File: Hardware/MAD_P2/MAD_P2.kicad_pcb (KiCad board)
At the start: 4 copper layers, 121.6 x 145.5 mm, 363 parts, among them J1 Line_1_3, J10 Conn_02x05_Odd_Even, J11 Conn_02x05_Odd_Even, J12 Line_3_3, J13 Conn_02x05_Odd_Even, J14 Conn_02x05_Odd_Even, J15 Conn_ADC1, J16 Conn_DAC, J17 Line_1_2, J18 P3, J19 P4, J2 Line_2_2, J20 P2, J21 Conn_02x05_Odd_Even, J22 Conn_02x05_Odd_Even, J23 Conn_02x03_Odd_Even, J24 P5, J25 P6, J26 P7, J27 Line_1_1, J28 Line_2_1, J29 Line_2_3, J3 Line_3_1, J30 Line_3_2, J31 Micro_SD_Card_Connector, J32 Micro_SD_Card_Socket, J33 Shifted IO, J4 Power_In, J5 Micro_SD_Card, J6 Edge_Conn, J7 Conn_02x05_Odd_Even, J8 USB_C_Receptacle_USB2.0, J9 Conn_02x05_Odd_Even, P10 CONN_01X01, P11 CONN_01X01, P13 CONN_01X01, P8 CONN_01X01, Q1 MMBT3904, Q2 2N7002, Q3 2N7002, Q4 2N7002, Q5 2N7002, SW1 Switch_SW_Push, U1 P2X8C4M64P-REF, U10 AMS1117-3.3, U11 APM4953, U12 APM4953, U13 XL1509-5.0, U14 XL1509-5.0, U15 AMS1117-3.3, U16 AMS1117-3.3, U17 MAX5134-7, U18 AMS1117-3.3, U19 AMS1117-1.8, U2 XL1509-5.0, U20 LM321, U21 APM4953, U22 XL1509-5.0, U23 ADS131A04, U24 AMS1117-3.3, U26 W25Q128JVS, U27 FT232RL, U28 DS3231M, U29 ESP-12F, U3 XL1509-5.0, U4 XL1509-5.0, U5 XL1509-5.0, U6 AMS1117-3.3, U7 AMS1117-3.3, U8 AMS1117-3.3, U9 AMS1117-3.3, Y1 20MHz, Y2 16.384MHz

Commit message: begining autorouter, had to start again after edge connector footprint was incorrect
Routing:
- net P22: track 0.00 -> 4.75 mm, vias 0 -> 1
- net GND: track 623.8 -> 619.0 mm, vias 343 -> 342
- net Net-(J8-PadA6): track 4.29 -> 6.99 mm
- net Net-(J8-PadA7): track 3.03 -> 5.73 mm

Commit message: added boarders along keep out zones for autorouter:
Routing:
- net (no net): track 0.00 -> 698.4 mm
- added copper zone on In1.Cu, net (none)
- removed copper zone on In1.Cu, net +1V8
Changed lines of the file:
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@@
     (thickness 1.6)
     (drawings 126)
-    (tracks 3104)
+    (tracks 3168)
     (zones 0)
     (modules 363)
@@
   (gr_line (start 514 160.867) (end 514 15.367) (layer Edge.Cuts) (width 0.05))
   (gr_line (start 392.43 160.867) (end 514 160.867) (layer Edge.Cuts) (width 0.05))
+  (segment (start 407.67 130.573166) (end 407.797 130.446166) (width 0.25) (layer F.Cu) (net 0))
+  (segment (start 407.67 153.67) (end 407.67 130.573166) (width 0.25) (layer F.Cu) (net 0))
+  (segment (start 407.797 130.446166) (end 407.797 120.5865) (width 0.25) (layer F.Cu) (net 0))
+  (segment (start 431.927 160.274) (end 431.927 156.0195) (width 0.25) (layer F.Cu) (net 0))
+  (segment (start 431.927 156.0195) (end 432.562 155.3845) (width 0.25) (layer F.Cu) (net 0))
+  (segment (start 432.562 155.3845) (end 432.562 118.5545) (width 0.25) (layer F.Cu) (net 0))
+  (segment (start 432.435 117.094) (end 410.6545 117.094) (width 0.25) (layer F.Cu) (net 0))
+  (segment (start 407.67 130.573166) (end 407.797 130.446166) (width 0.25) (layer F.Cu) (net 0))
+  (segment (start 432.435 117.094) (end 410.6545 117.094) (width 0.25) (layer F.Cu) (net 0))
+  (segment (start 432.562 155.3845) (end 432.562 118.5545) (width 0.25) (layer F.Cu) (net 0))
+  (segment (start 407.67 153.67) (end 407.67 130.573166) (width 0.25) (layer F.Cu) (net 0))
+  (segment (start 407.797 130.446166) (end 407.797 120.5865) (width 0.25) (layer F.Cu) (net 0))
+  (segment (start 407.8605 153.67) (end 407.8605 117.2845) (width 0.25) (layer In1.Cu) (net 0))
+  (segment (start 407.8605 117.2845) (end 432.3715 117.2845) (width 0.25) (layer In1.Cu) (net 0))
+  (segment (start 432.91649 117.82949) (end 432.91649 133.18601) (width 0.25) (layer In1.Cu) (net 0))
+  (segment (start 432.3715 117.2845) (end 432.91649 117.82949) (width 0.25) (layer In1.Cu) (net 0))
+  (segment (start 432.91649 151.874808) (end 431.8635 152.927798) (width 0.25) (layer In1.Cu) (net 0))
+  (segment (start 432.91649 133.18601) (end 432.91649 151.874808) (width 0.25) (layer In1.Cu) (net 0))
+  (segment (start 431.8635 152.927798) (end 431.8635 160.0835) (width 0.25) (layer In1.Cu) (net 0))
+  (segment (start 407.4795 144.278498) (end 407.8605 143.897498) (width 0.25) (layer In2.Cu) (net 0))
+  (segment (start 407.4795 153.7335) (end 407.4795 144.278498) (width 0.25) (layer In2.Cu) (net 0))
+  (segment (start 407.8605 143.897498) (end 407.8605 119.247498) (width 0.25) (layer In2.Cu) (net 0))
+  (segment (start 407.8605 119.247498) (end 409.823498 117.2845) (width 0.25) (layer In2.Cu) (net 0))
+  (segment (start 409.823498 117.2845) (end 432.4985 117.2845) (width 0.25) (layer In2.Cu) (net 0))
+  (segment (start 432.4985 118.230502) (end 432.7525 118.484502) (width 0.25) (layer In2.Cu) (net 0))
+  (segment (start 432.4985 117.2845) (end 432.4985 118.230502) (width 0.25) (layer In2.Cu) (net 0))
+  (segment (start 432.7525 159.639) (end 431.87451 160.51699) (width 0.25) (layer In2.Cu) (net 0))
+  (segment (start 432.7525 118.484502) (end 432.7525 159.639) (width 0.25) (layer In2.Cu) (net 0))
+  (segment (start 407.797 154.1145) (end 407.797 127.831998) (width 0.25) (layer B.Cu) (net 0))
+  (segment (start 407.797 119.310998) (end 409.823498 117.2845) (width 0.25) (layer B.Cu) (net 0))
+  (segment (start 407.797 127.831998) (end 407.797 119.310998) (width 0.25) (layer B.Cu) (net 0))
+  (segment (start 409.823498 117.2845) (end 432.054 117.2845) (width 0.25) (layer B.Cu) (net 0))
+  (segment (start 432.537501 117.768001) (end 432.537501 159.028499) (width 0.25) (layer B.Cu) (net 0))
+  (segment (start 432.054 117.2845) (end 432.537501 117.768001) (width 0.25) (layer B.Cu) (net 0))
+  (segment (start 452.4375 135.6995) (end 445.262 135.6995) (width 0.25) (layer B.Cu) (net 0))
+  (segment (start 445.262 135.6995) (end 445.262 116.1415) (width 0.25) (layer B.Cu) (net 0))
+  (segment (start 445.362499 116.041001) (end 464.910001 116.041001) (width 0.25) (layer B.Cu) (net 0))
+  (segment (start 445.262 116.1415) (end 445.362499 116.041001) (width 0.25) (layer B.Cu) (net 0))
+  (segment (start 464.910001 116.041001) (end 465.201 116.332) (width 0.25) (layer B.Cu) (net 0))
+  (segment (start 465.201 131.372002) (end 465.1375 131.435502) (width 0.25) (layer B.Cu) (net 0))
+  (segment (start 465.201 116.332) (end 465.201 131.372002) (width 0.25) (layer B.Cu) (net 0))
+  (segment (start 465.1375 131.435502) (end 465.1375 135.5725) (width 0.25) (layer B.Cu) (net 0))
+  (segment (start 465.1375 135.5725) (end 457.327 135.5725) (width 0.25) (layer B.Cu) (net 0))
+  (segment (start 452.755 135.763) (end 445.262 135.763) (width 0.25) (layer In2.Cu) (net 0))
+  (segment (start 445.262 135.763) (end 445.135 135.636) (width 0.25) (layer In2.Cu) (net 0))
+  (segment (start 445.135 122.612998) (end 451.669998 116.078) (width 0.25) (layer In2.Cu) (net 0))
+  (segment (start 445.135 135.636) (end 445.135 122.612998) (width 0.25) (layer In2.Cu) (net 0))
+  (segment (start 451.669998 116.078) (end 458.794002 116.078) (width 0.25) (layer In2.Cu) (net 0))
+  (segment (start 458.794002 116.078) (end 458.921002 116.205) (width 0.25) (layer In2.Cu) (net 0))
+  (segment (start 458.921002 116.205) (end 465.2645 116.205) (width 0.25) (layer In2.Cu) (net 0))
+  (segment (start 465.2645 116.205) (end 465.0105 116.459) (width 0.25) (layer In2.Cu) (net 0))
+  (segment (start 465.0105 116.459) (end 465.0105 131.562502) (width 0.25) (layer In2.Cu) (net 0))
+  (segment (start 465.0105 131.562502) (end 465.0105 135.382) (width 0.25) (layer In2.Cu) (net 0))
+  (segment (start 465.0105 135.382) (end 464.693 135.6995) (width 0.25) (layer In2.Cu) (net 0))
+  (segment (start 464.693 135.6995) (end 457.327 135.6995) (width 0.25) (layer In2.Cu) (net 0))
+  (segment (start 452.755 136.0805) (end 445.262 136.0805) (width 0.25) (layer F.Cu) (net 0))
+  (segment (start 457.3905 136.144) (end 464.947 136.144) (width 0.25) (layer F.Cu) (net 0))
+  (segment (start 464.947 136.144) (end 465.836 135.255) (width 0.25) (layer F.Cu) (net 0))
+  (segment (start 465.836 135.255) (end 465.836 122.483588) (width 0.25) (layer F.Cu) (net 0))
+  (segment (start 465.836 122.483588) (end 465.836 117.1575) (width 0.25) (layer F.Cu) (net 0))
+  (segment (start 453.733412 116.84) (end 453.542912 117.0305) (width 0.25) (layer F.Cu) (net 0))
+  (segment (start 465.5185 116.84) (end 453.733412 116.84) (width 0.25) (layer F.Cu) (net 0))
+  (segment (start 465.836 117.1575) (end 465.5185 116.84) (width 0.25) (layer F.Cu) (net 0))
+  (segment (start 453.542912 117.0305) (end 445.3255 117.0305) (width 0.25) (layer F.Cu) (net 0))
   (via (at 479.8125 144.9375) (size 0.8) (drill 0.4) (layers F.Cu B.Cu) (net 1))
   (segment (start 472.91699 138.04199) (end 479.8125 144.9375) (width 0.25) (layer F.Cu) (net 1))
@@
     )
   )
-  (zone (net 3) (net_name +1V8) (layer In1.Cu) (hatch edge 0.508)
+  (zone (net 0) (net_name "") (layer In1.Cu) (hatch edge 0.508)
     (connect_pads (clearance 0.508))
     (min_thickness 0.254)

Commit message: added keepout areas to adc/dac
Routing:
- net (no net): track 698.4 -> 0.00 mm
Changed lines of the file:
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@@
     (thickness 1.6)
     (drawings 126)
-    (tracks 3168)
+    (tracks 3104)
     (zones 0)
     (modules 363)
@@
   (gr_line (start 514 160.867) (end 514 15.367) (layer Edge.Cuts) (width 0.05))
   (gr_line (start 392.43 160.867) (end 514 160.867) (layer Edge.Cuts) (width 0.05))
-  (segment (start 407.67 130.573166) (end 407.797 130.446166) (width 0.25) (layer F.Cu) (net 0))
-  (segment (start 407.67 153.67) (end 407.67 130.573166) (width 0.25) (layer F.Cu) (net 0))
-  (segment (start 407.797 130.446166) (end 407.797 120.5865) (width 0.25) (layer F.Cu) (net 0))
-  (segment (start 431.927 160.274) (end 431.927 156.0195) (width 0.25) (layer F.Cu) (net 0))
-  (segment (start 431.927 156.0195) (end 432.562 155.3845) (width 0.25) (layer F.Cu) (net 0))
-  (segment (start 432.562 155.3845) (end 432.562 118.5545) (width 0.25) (layer F.Cu) (net 0))
-  (segment (start 432.435 117.094) (end 410.6545 117.094) (width 0.25) (layer F.Cu) (net 0))
-  (segment (start 407.67 130.573166) (end 407.797 130.446166) (width 0.25) (layer F.Cu) (net 0))
-  (segment (start 432.435 117.094) (end 410.6545 117.094) (width 0.25) (layer F.Cu) (net 0))
-  (segment (start 432.562 155.3845) (end 432.562 118.5545) (width 0.25) (layer F.Cu) (net 0))
-  (segment (start 407.67 153.67) (end 407.67 130.573166) (width 0.25) (layer F.Cu) (net 0))
-  (segment (start 407.797 130.446166) (end 407.797 120.5865) (width 0.25) (layer F.Cu) (net 0))
-  (segment (start 407.8605 153.67) (end 407.8605 117.2845) (width 0.25) (layer In1.Cu) (net 0))
-  (segment (start 407.8605 117.2845) (end 432.3715 117.2845) (width 0.25) (layer In1.Cu) (net 0))
-  (segment (start 432.91649 117.82949) (end 432.91649 133.18601) (width 0.25) (layer In1.Cu) (net 0))
-  (segment (start 432.3715 117.2845) (end 432.91649 117.82949) (width 0.25) (layer In1.Cu) (net 0))
-  (segment (start 432.91649 151.874808) (end 431.8635 152.927798) (width 0.25) (layer In1.Cu) (net 0))
-  (segment (start 432.91649 133.18601) (end 432.91649 151.874808) (width 0.25) (layer In1.Cu) (net 0))
-  (segment (start 431.8635 152.927798) (end 431.8635 160.0835) (width 0.25) (layer In1.Cu) (net 0))
-  (segment (start 407.4795 144.278498) (end 407.8605 143.897498) (width 0.25) (layer In2.Cu) (net 0))
-  (segment (start 407.4795 153.7335) (end 407.4795 144.278498) (width 0.25) (layer In2.Cu) (net 0))
-  (segment (start 407.8605 143.897498) (end 407.8605 119.247498) (width 0.25) (layer In2.Cu) (net 0))
-  (segment (start 407.8605 119.247498) (end 409.823498 117.2845) (width 0.25) (layer In2.Cu) (net 0))
-  (segment (start 409.823498 117.2845) (end 432.4985 117.2845) (width 0.25) (layer In2.Cu) (net 0))
-  (segment (start 432.4985 118.230502) (end 432.7525 118.484502) (width 0.25) (layer In2.Cu) (net 0))
-  (segment (start 432.4985 117.2845) (end 432.4985 118.230502) (width 0.25) (layer In2.Cu) (net 0))
-  (segment (start 432.7525 159.639) (end 431.87451 160.51699) (width 0.25) (layer In2.Cu) (net 0))
-  (segment (start 432.7525 118.484502) (end 432.7525 159.639) (width 0.25) (layer In2.Cu) (net 0))
-  (segment (start 407.797 154.1145) (end 407.797 127.831998) (width 0.25) (layer B.Cu) (net 0))
-  (segment (start 407.797 119.310998) (end 409.823498 117.2845) (width 0.25) (layer B.Cu) (net 0))
-  (segment (start 407.797 127.831998) (end 407.797 119.310998) (width 0.25) (layer B.Cu) (net 0))
-  (segment (start 409.823498 117.2845) (end 432.054 117.2845) (width 0.25) (layer B.Cu) (net 0))
-  (segment (start 432.537501 117.768001) (end 432.537501 159.028499) (width 0.25) (layer B.Cu) (net 0))
-  (segment (start 432.054 117.2845) (end 432.537501 117.768001) (width 0.25) (layer B.Cu) (net 0))
-  (segment (start 452.4375 135.6995) (end 445.262 135.6995) (width 0.25) (layer B.Cu) (net 0))
-  (segment (start 445.262 135.6995) (end 445.262 116.1415) (width 0.25) (layer B.Cu) (net 0))
-  (segment (start 445.362499 116.041001) (end 464.910001 116.041001) (width 0.25) (layer B.Cu) (net 0))
-  (segment (start 445.262 116.1415) (end 445.362499 116.041001) (width 0.25) (layer B.Cu) (net 0))
-  (segment (start 464.910001 116.041001) (end 465.201 116.332) (width 0.25) (layer B.Cu) (net 0))
-  (segment (start 465.201 131.372002) (end 465.1375 131.435502) (width 0.25) (layer B.Cu) (net 0))
-  (segment (start 465.201 116.332) (end 465.201 131.372002) (width 0.25) (layer B.Cu) (net 0))
-  (segment (start 465.1375 131.435502) (end 465.1375 135.5725) (width 0.25) (layer B.Cu) (net 0))
-  (segment (start 465.1375 135.5725) (end 457.327 135.5725) (width 0.25) (layer B.Cu) (net 0))
-  (segment (start 452.755 135.763) (end 445.262 135.763) (width 0.25) (layer In2.Cu) (net 0))
-  (segment (start 445.262 135.763) (end 445.135 135.636) (width 0.25) (layer In2.Cu) (net 0))
-  (segment (start 445.135 122.612998) (end 451.669998 116.078) (width 0.25) (layer In2.Cu) (net 0))
-  (segment (start 445.135 135.636) (end 445.135 122.612998) (width 0.25) (layer In2.Cu) (net 0))
-  (segment (start 451.669998 116.078) (end 458.794002 116.078) (width 0.25) (layer In2.Cu) (net 0))
-  (segment (start 458.794002 116.078) (end 458.921002 116.205) (width 0.25) (layer In2.Cu) (net 0))
-  (segment (start 458.921002 116.205) (end 465.2645 116.205) (width 0.25) (layer In2.Cu) (net 0))
-  (segment (start 465.2645 116.205) (end 465.0105 116.459) (width 0.25) (layer In2.Cu) (net 0))
-  (segment (start 465.0105 116.459) (end 465.0105 131.562502) (width 0.25) (layer In2.Cu) (net 0))
-  (segment (start 465.0105 131.562502) (end 465.0105 135.382) (width 0.25) (layer In2.Cu) (net 0))
-  (segment (start 465.0105 135.382) (end 464.693 135.6995) (width 0.25) (layer In2.Cu) (net 0))
-  (segment (start 464.693 135.6995) (end 457.327 135.6995) (width 0.25) (layer In2.Cu) (net 0))
-  (segment (start 452.755 136.0805) (end 445.262 136.0805) (width 0.25) (layer F.Cu) (net 0))
-  (segment (start 457.3905 136.144) (end 464.947 136.144) (width 0.25) (layer F.Cu) (net 0))
-  (segment (start 464.947 136.144) (end 465.836 135.255) (width 0.25) (layer F.Cu) (net 0))
-  (segment (start 465.836 135.255) (end 465.836 122.483588) (width 0.25) (layer F.Cu) (net 0))
-  (segment (start 465.836 122.483588) (end 465.836 117.1575) (width 0.25) (layer F.Cu) (net 0))
-  (segment (start 453.733412 116.84) (end 453.542912 117.0305) (width 0.25) (layer F.Cu) (net 0))
-  (segment (start 465.5185 116.84) (end 453.733412 116.84) (width 0.25) (layer F.Cu) (net 0))
-  (segment (start 465.836 117.1575) (end 465.5185 116.84) (width 0.25) (layer F.Cu) (net 0))
-  (segment (start 453.542912 117.0305) (end 445.3255 117.0305) (width 0.25) (layer F.Cu) (net 0))
   (via (at 479.8125 144.9375) (size 0.8) (drill 0.4) (layers F.Cu B.Cu) (net 1))
   (segment (start 472.91699 138.04199) (end 479.8125 144.9375) (width 0.25) (layer F.Cu) (net 1))
@@
       )
     )
+  )
+  (zone (net 0) (net_name "") (layers F.Cu In1.Cu In2.Cu B.Cu) (hatch edge 0.508)
+    (connect_pads (clearance 0.508))
+    (min_thickness 0.254)
+    (keepout (tracks not_allowed) (vias not_allowed) (copperpour allowed))
+    (fill (arc_segments 32) (thermal_gap 0.508) (thermal_bridge_width 0.508))
+    (polygon
+      (pts
+        (xy 432.7525 160.8455) (xy 407.6065 160.8455) (xy 407.6065 116.967) (xy 432.7525 116.967)
+      )
+    )
+  )
+  (zone (net 0) (net_name "") (layers F.Cu In1.Cu In2.Cu B.Cu) (hatch edge 0.508)
+    (connect_pads (clearance 0.508))
+    (min_thickness 0.254)
+    (keepout (tracks not_allowed) (vias not_allowed) (copperpour allowed))
+    (fill (arc_segments 32) (thermal_gap 0.508) (thermal_bridge_width 0.508))
+    (polygon
+      (pts
+        (xy 465.201 135.509) (xy 445.262 135.5725) (xy 445.3255 116.3955) (xy 465.201 116.3955)
+      )
+    )

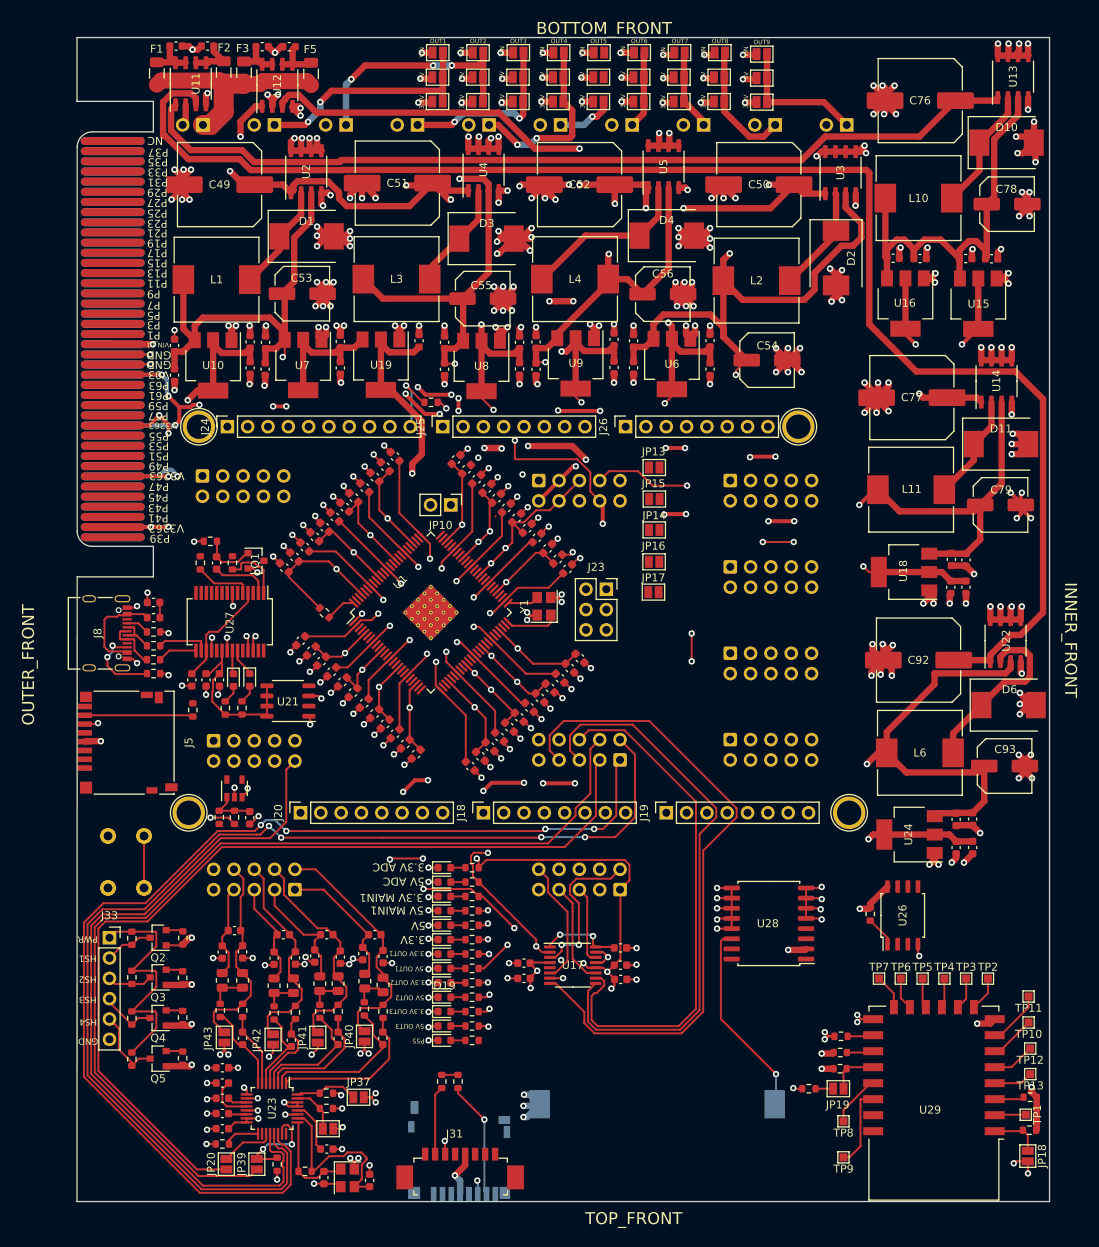
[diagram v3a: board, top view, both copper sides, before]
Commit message: added silkscreen
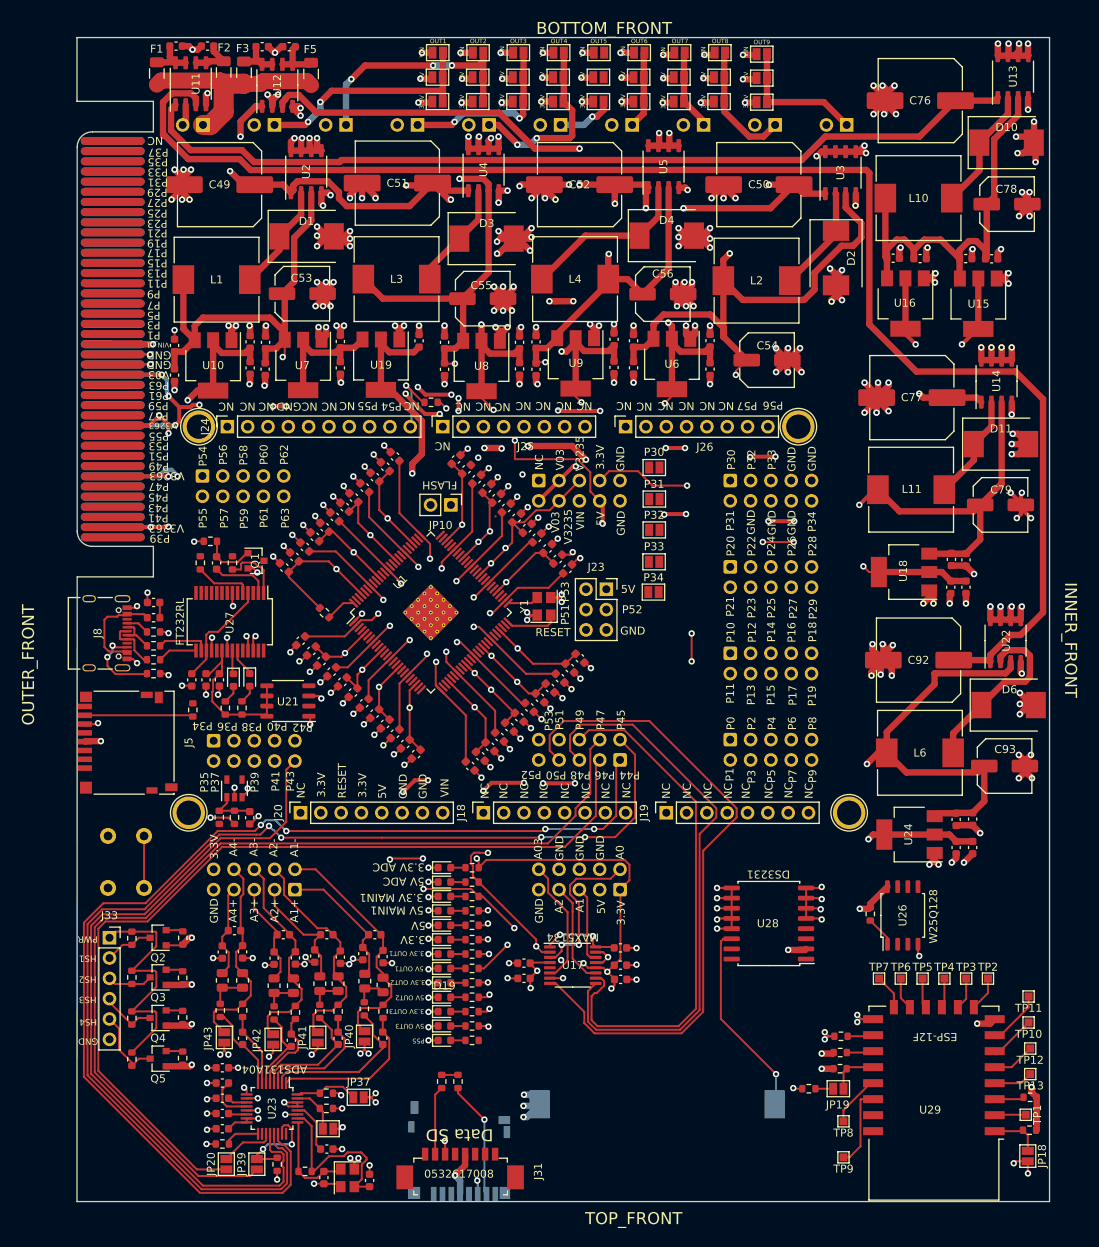
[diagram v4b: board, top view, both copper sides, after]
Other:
- board text added: "0532617008"
- board text added: "A0"
- board text added: "A03"
- board text added: "A1"
- board text added: "A1+"
- board text added: "A1-"
- board text added: "A2"
- board text added: "A2+"
- board text added: "A2-"
- board text added: "A3+"
- board text added: "A3-"
- board text added: "A4+"
- board text added: "A4-"
- board text added: "ADC"
- board text added: "ADS131A04"
- board text added: "CR2032"
- board text added: "DS3231"
- board text added: "Data SD"
- board text added: "ESP-12F"
- board text added: "FLASH"
- board text added: "FT232RL"
- board text added: "MAX5134"
- board text added: "P0"
- board text added: "P10"
- board text added: "P12"
- board text added: "P14"
- board text added: "P16"
- board text added: "P18"
- board text added: "P2"
- board text added: "P20"
- board text added: "P22"
- board text added: "P24"
- board text added: "P26"
- board text added: "P28"
- board text added: "P38"
- board text added: "P4"
- board text added: "P40"
- board text added: "P42"
- board text added: "P44"
- board text added: "P46"
- board text added: "P48"
- board text added: "P50"
- board text added: "P52"
- board text added: "P54"
- board text added: "P56"
- board text added: "P58"
- board text added: "P6"
- board text added: "P60"
- board text added: "P62"
- board text added: "P8"
- board text added: "RESET"
- board text added: "V1619"
- board text added: "V2427"
- board text added: "V3235"
- board text added: "V4043"
- board text added: "V4851"
- board text added: "V5659"
- board text added: "V811"
- board text added: "W25Q128"
